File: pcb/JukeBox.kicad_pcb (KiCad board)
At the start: 2 copper layers, 102 x 100 mm, 102 parts, among them J1 USB_C_Receptacle_USB2.0_16P, Q1 Q_NPN_BEC, SW1 SW_SPST, SW10 SW_SPST, SW11 SW_SPST, SW12 SW_SPST, SW13 SW_SPST, SW2 SW_SPST, SW3 SW_SPST, SW4 SW_SPST, SW5 SW_SPST, SW6 SW_SPST, SW7 SW_SPST, SW8 SW_SPST, SW9 SW_SPST, U1 NCP1117-3.3_SOT223, U2 W25Q128JVS, U3 RP2350_60QFN, U5 CAT24C512, Y1 ABM8-272-T3

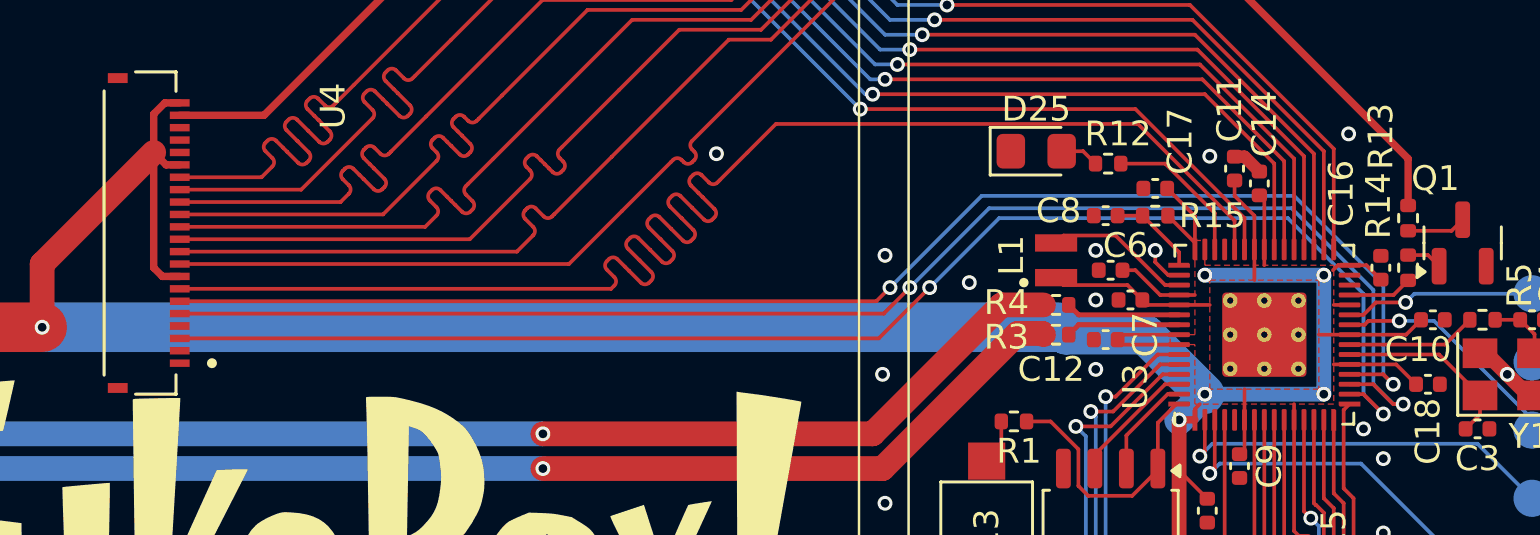
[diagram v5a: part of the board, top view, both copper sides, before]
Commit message: update pcb to add missing pin for screen
ugh
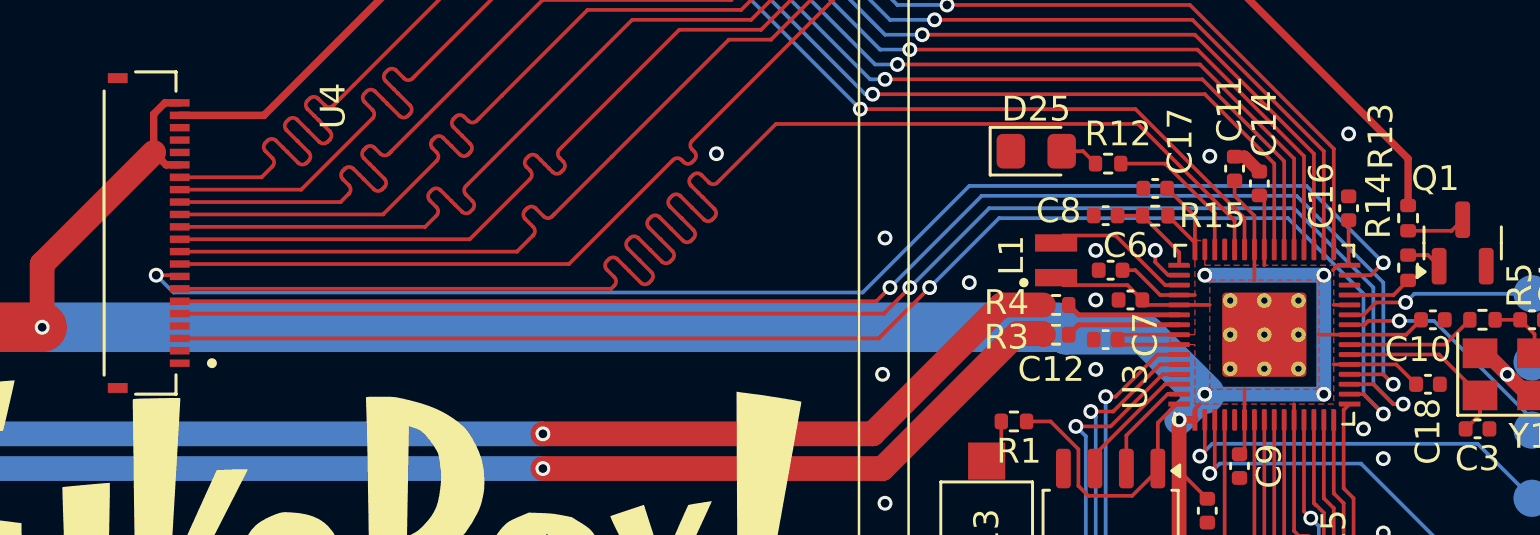
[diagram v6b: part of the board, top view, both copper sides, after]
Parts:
- moved C16 2.73 mm to (153.6, 82.7)
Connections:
- U3 pad 29: /GPIO18 -> /SCRRD
- U4 pad 15: +3V3 -> /SCRRD
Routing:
- net /SCRRD: track 0.00 -> 55.4 mm, vias 0 -> 2
- net +3V3: track 167.1 -> 161.5 mm

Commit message: DNP updates for BOM
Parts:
- moved C15 2.90 mm to (151.8, 93.7)
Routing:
- net +3V3: track 161.5 -> 158.6 mm
- net /KBROW3: vias 4 -> 2
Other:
- board text added: "v5.9 - F.T.I. <3 (c) 2020-2025 https://jukebox.friendteam.biz"
- board text removed: "v5.8 - F.T.I. <3 (c) 2020-2025 https://jukebox.friendteam.biz"
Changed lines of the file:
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@@
 		(tags "capacitor")
 		(property "Reference" "C9"
-			(at 0 -1.2 90)
+			(at 1.9 0 90)
 			(layer "F.SilkS")
 			(effects
@@
 	(footprint "Capacitor_SMD:C_0402_1005Metric"
 		(layer "F.Cu")
-		(at 151.79 96.6 -90)
+		(at 151.79 93.7 -90)
 		(descr "Capacitor SMD 0402 (1005 Metric), square (rectangular) end terminal, IPC_7351 nominal, (Body size source: IPC-SM-782 page 76, https://www.pcb-3d.com/wordpress/wp-content/uploads/ipc-sm-782a_amendment_1_and_2.pdf), generated with kicad-footprint-generator")
 		(tags "capacitor")
 		(property "Reference" "C15"
-			(at -0.4 -1.2 90)
+			(at 2.5 0 90)
 			(layer "F.SilkS")
 			(effects
@@
 		(layer "Edge.Cuts")
 	)
-	(gr_text "v5.8 - F.T.I. <3 (c) 2020-2025\nhttps://jukebox.friendteam.biz"
+	(gr_text "v5.9 - F.T.I. <3 (c) 2020-2025\nhttps://jukebox.friendteam.biz"
 		(at 112.59 164 0)
 		(layer "B.SilkS")
@@
 		)
 	)
-	(gr_text "v5.8 - F.T.I. <3 (c) 2020-2025\nhttps://jukebox.friendteam.biz"
+	(gr_text "v5.9 - F.T.I. <3 (c) 2020-2025\nhttps://jukebox.friendteam.biz"
 		(at 112.59 164 0)
 		(layer "F.SilkS")
@@
 	)
 	(via
+		(at 151.69 98.3)
+		(size 0.6)
+		(drill 0.35)
+		(layers "F.Cu" "B.Cu")
+		(free yes)
+		(net 1)
+	)
+	(via
 		(at 122.59 141.85)
 		(size 0.6)
@@
 	)
 	(via
-		(at 151.79 98)
-		(size 0.6)
-		(drill 0.35)
-		(layers "F.Cu" "B.Cu")
-		(free yes)
-		(net 1)
-	)
-	(via
 		(at 145.79 84.4)
 		(size 0.6)
@@
 	)
 	(segment
-		(start 151.39 95.72)
-		(end 151.79 96.12)
+		(start 151.79 92.8)
+		(end 151.79 93.22)
 		(width 0.15)
 		(layer "F.Cu")
@@
 	)
 	(segment
+		(start 151.39 91.2375)
+		(end 151.39 92.4)
+		(width 0.15)
+		(layer "F.Cu")
+		(net 5)
+	)
+	(segment
 		(start 146.7525 86.2)
 		(end 147.39 86.2)
@@
 	)
 	(segment
+		(start 151.39 92.4)
+		(end 151.79 92.8)
+		(width 0.15)
+		(layer "F.Cu")
+		(net 5)
+	)
+	(segment
 		(start 153.6275 89)
 		(end 155.51 89)
@@
 	)
 	(segment
-		(start 151.39 91.2375)
-		(end 151.39 95.72)
-		(width 0.15)
-		(layer "F.Cu")
-		(net 5)
-	)
-	(segment
 		(start 145.99 86.2)
 		(end 144.99 85.2)
@@
 	)
 	(segment
-		(start 152.84 144.05)
-		(end 151.29 145.6)
+		(start 152.84 105)
+		(end 152.09 104.25)
 		(width 0.15)
 		(layer "F.Cu")
@@
 	)
 	(segment
-		(start 151.29 145.6)
-		(end 149.99 145.6)
+		(start 152.39 92.8)
+		(end 151.79 92.2)
 		(width 0.15)
 		(layer "F.Cu")
@@
 	)
 	(segment
-		(start 151.79 99.05)
-		(end 149.49 101.35)
+		(start 152.09 104.25)
+		(end 150.34 104.25)
 		(width 0.15)
 		(layer "F.Cu")
@@
 	)
 	(segment
-		(start 149.49 103.4)
-		(end 150.34 104.25)
+		(start 150.34 104.25)
+		(end 149.49 103.4)
 		(width 0.15)
 		(layer "F.Cu")
@@
 	)
 	(segment
-		(start 152.84 105)
-		(end 152.84 144.05)
+		(start 152.84 144.05)
+		(end 152.84 105)
 		(width 0.15)
 		(layer "F.Cu")
@@
 	)
 	(segment
-		(start 151.79 98.8)
-		(end 151.79 99.05)
+		(start 151.29 145.6)
+		(end 149.99 145.6)
 		(width 0.15)
 		(layer "F.Cu")
@@
 	)
 	(segment
-		(start 150.34 104.25)
-		(end 152.09 104.25)
+		(start 149.49 101.5)
+		(end 152.39 98.6)
 		(width 0.15)
 		(layer "F.Cu")
@@
 	)
 	(segment
-		(start 152.09 104.25)
-		(end 152.84 105)
+		(start 151.79 92.2)
+		(end 151.79 91.2375)
 		(width 0.15)
 		(layer "F.Cu")
@@
 	)
 	(segment
-		(start 111.29 145.6)
-		(end 131.29 145.6)
+		(start 149.49 103.4)
+		(end 149.49 101.5)
 		(width 0.15)
 		(layer "F.Cu")
@@
 	)
 	(segment
-		(start 152.065 95.2)
-		(end 151.79 94.925)
+		(start 111.29 145.6)
+		(end 131.29 145.6)
 		(width 0.15)
 		(layer "F.Cu")
@@
 	)
 	(segment
-		(start 149.49 101.35)
-		(end 149.49 103.4)
+		(start 151.29 145.6)
+		(end 152.84 144.05)
 		(width 0.15)
 		(layer "F.Cu")
@@
 	)
 	(segment
-		(start 151.79 94.925)
-		(end 151.79 91.2375)
+		(start 152.39 98.6)
+		(end 152.39 92.8)
 		(width 0.15)
 		(layer "F.Cu")
@@
 		(net 10)
 	)
-	(via
-		(at 151.79 98.8)
-		(size 0.6)
-		(drill 0.35)
-		(layers "F.Cu" "B.Cu")
-		(net 10)
-	)
-	(via
-		(at 152.065 95.2)
-		(size 0.6)
-		(drill 0.35)
-		(layers "F.Cu" "B.Cu")
-		(net 10)
-	)
-	(segment
-		(start 152.39 95.525)
-		(end 152.39 98.2)
-		(width 0.15)
-		(layer "B.Cu")
-		(net 10)
-	)
 	(segment
 		(start 149.99 145.6)
@@
 	)
 	(segment
-		(start 152.39 98.2)
-		(end 151.79 98.8)
-		(width 0.15)
-		(layer "B.Cu")
-		(net 10)
-	)
-	(segment
-		(start 152.065 95.2)
-		(end 152.39 95.525)
-		(width 0.15)
-		(layer "B.Cu")
-		(net 10)
-	)
-	(segment
 		(start 143.555 107.75)
 		(end 143.505 107.8)
@@
 	)
 	(segment
-		(start 152.19 91.2375)
-		(end 152.19 94.6)
-		(width 0.15)
-		(layer "F.Cu")
-		(net 12)
-	)
-	(segment
-		(start 152.265 94.675)
-		(end 152.282463 94.675)
+		(start 152.79 99.05)
+		(end 150.09 101.75)
 		(width 0.15)
 		(layer "F.Cu")
@@
 	)
 	(segment
-		(start 152.59 94.982537)
-		(end 152.59 99.25)
+		(start 152.19 91.2375)
+		(end 152.19 92.1)
 		(width 0.15)
 		(layer "F.Cu")
@@
 	)
 	(segment
-		(start 75.97 156.1)
-		(end 74.84 157.23)
+		(start 152.19 92.1)
+		(end 152.79 92.7)
 		(width 0.15)
 		(layer "F.Cu")
@@
 	)
 	(segment
-		(start 152.282463 94.675)
-		(end 152.59 94.982537)
+		(start 152.79 92.7)
+		(end 152.79 99.05)
 		(width 0.15)
 		(layer "F.Cu")
@@
 	)
 	(segment
-		(start 152.19 94.6)
-		(end 152.265 94.675)
+		(start 75.97 156.1)
+		(end 74.84 157.23)
 		(width 0.15)
 		(layer "F.Cu")
@@
 		(net 12)
 	)
-	(segment
-		(start 152.59 99.25)
-		(end 150.09 101.75)
-		(width 0.15)
-		(layer "F.Cu")
-		(net 12)
-	)
 	(via
 		(at 150.09 101.75)
@@
 	)
 	(segment
-		(start 152.59 94.4)
+		(start 152.59 91.95)
 		(end 152.59 91.2375)
 		(width 0.15)
@@
 	(segment
 		(start 150.84 101.75)
-		(end 152.99 99.6)
+		(end 153.29 99.3)
 		(width 0.15)
 		(layer "F.Cu")
@@
 	)
 	(segment
-		(start 152.99 99.6)
-		(end 152.99 94.8)
+		(start 153.29 99.3)
+		(end 153.29 92.65)
 		(width 0.15)
 		(layer "F.Cu")
@@
 	)
 	(segment
-		(start 152.99 94.8)
-		(end 152.59 94.4)
+		(start 153.29 92.65)
+		(end 152.59 91.95)
 		(width 0.15)
 		(layer "F.Cu")
@@
 	)
 	(segment
-		(start 151.59 101.75)
-		(end 153.39 99.95)
+		(start 117.89 156.1)
+		(end 115.98 156.1)
 		(width 0.15)
 		(layer "F.Cu")
@@
 	)
 	(segment
-		(start 117.89 156.1)
-		(end 115.98 156.1)
+		(start 153.69 92.55)
+		(end 152.99 91.85)
 		(width 0.15)
 		(layer "F.Cu")
@@
 	)
 	(segment
-		(start 153.39 94.6)
-		(end 152.99 94.2)
+		(start 153.69 99.65)
+		(end 153.69 92.55)
 		(width 0.15)
 		(layer "F.Cu")
@@
 	)
 	(segment
-		(start 152.99 94.2)
-		(end 152.99 91.2375)
+		(start 115.98 156.1)
+		(end 114.84 157.24)
 		(width 0.15)
 		(layer "F.Cu")
@@
 	)
 	(segment
-		(start 115.98 156.1)
-		(end 114.84 157.24)
+		(start 152.99 91.85)
+		(end 152.99 91.2375)
 		(width 0.15)
 		(layer "F.Cu")
@@
 	)
 	(segment
-		(start 153.39 99.95)
-		(end 153.39 94.6)
+		(start 151.59 101.75)
+		(end 153.69 99.65)
 		(width 0.15)
 		(layer "F.Cu")
@@
 	)
 	(segment
-		(start 153.79 94.4)
-		(end 153.79 100.3)
-		(width 0.15)
-		(layer "F.Cu")
-		(net 15)
-	)
-	(segment
-		(start 153.79 100.3)
-		(end 152.34 101.75)
+		(start 154.09 92.4)
+		(end 154.09 100)
 		(width 0.15)
 		(layer "F.Cu")
@@
 	)
 	(segment
-		(start 153.39 90.8375)
-		(end 153.39 94)
+		(start 153.6275 90.6)
+		(end 153.6275 91.9375)
 		(width 0.15)
 		(layer "F.Cu")
@@
 	)
 	(segment
-		(start 153.6275 90.6)
-		(end 153.39 90.8375)
+		(start 153.6275 91.9375)
+		(end 154.09 92.4)
 		(width 0.15)
 		(layer "F.Cu")
@@
 	)
 	(segment
-		(start 153.39 94)
-		(end 153.79 94.4)
+		(start 154.09 100)
+		(end 152.34 101.75)
 		(width 0.15)
 		(layer "F.Cu")
